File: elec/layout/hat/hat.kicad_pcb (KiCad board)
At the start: 4 copper layers, 108 x 115.9 mm, 85 parts

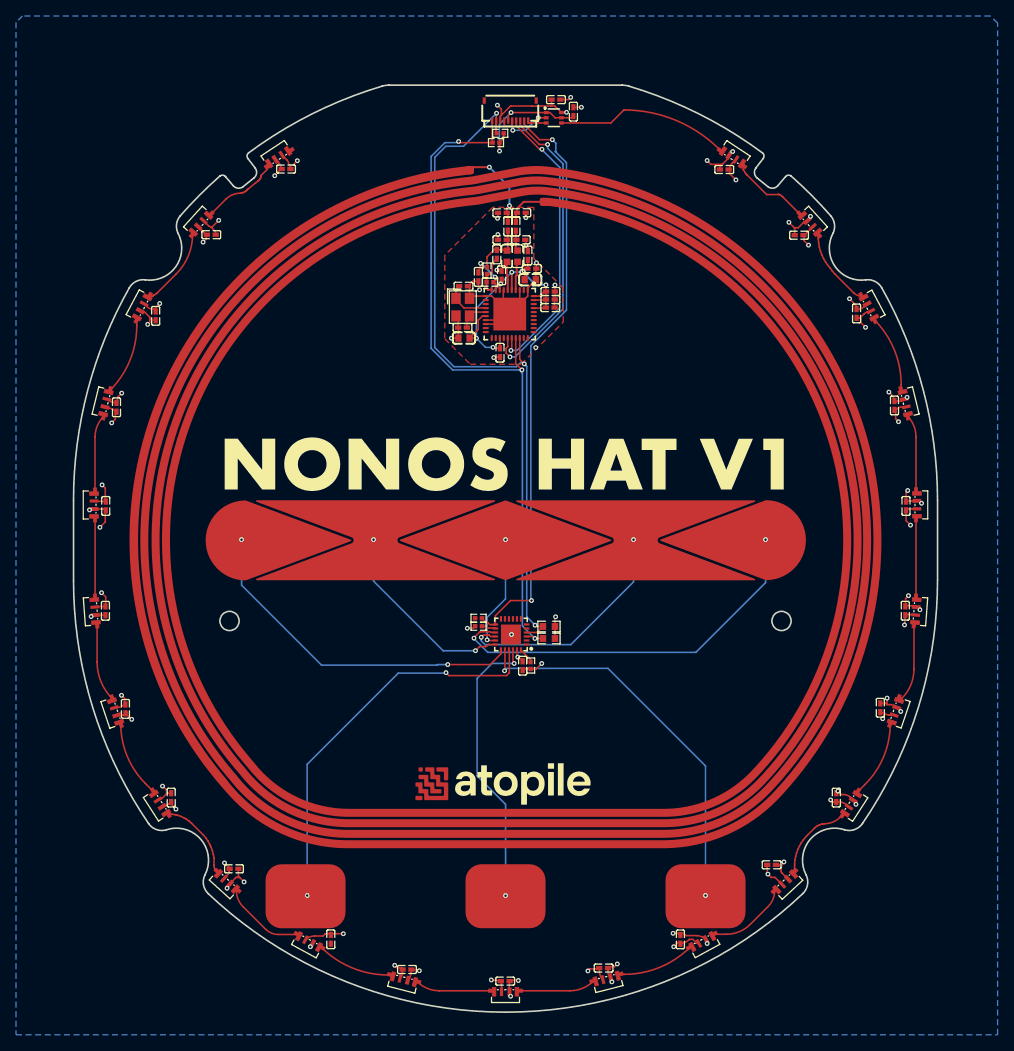
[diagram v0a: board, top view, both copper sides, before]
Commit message: fix via in pad issue
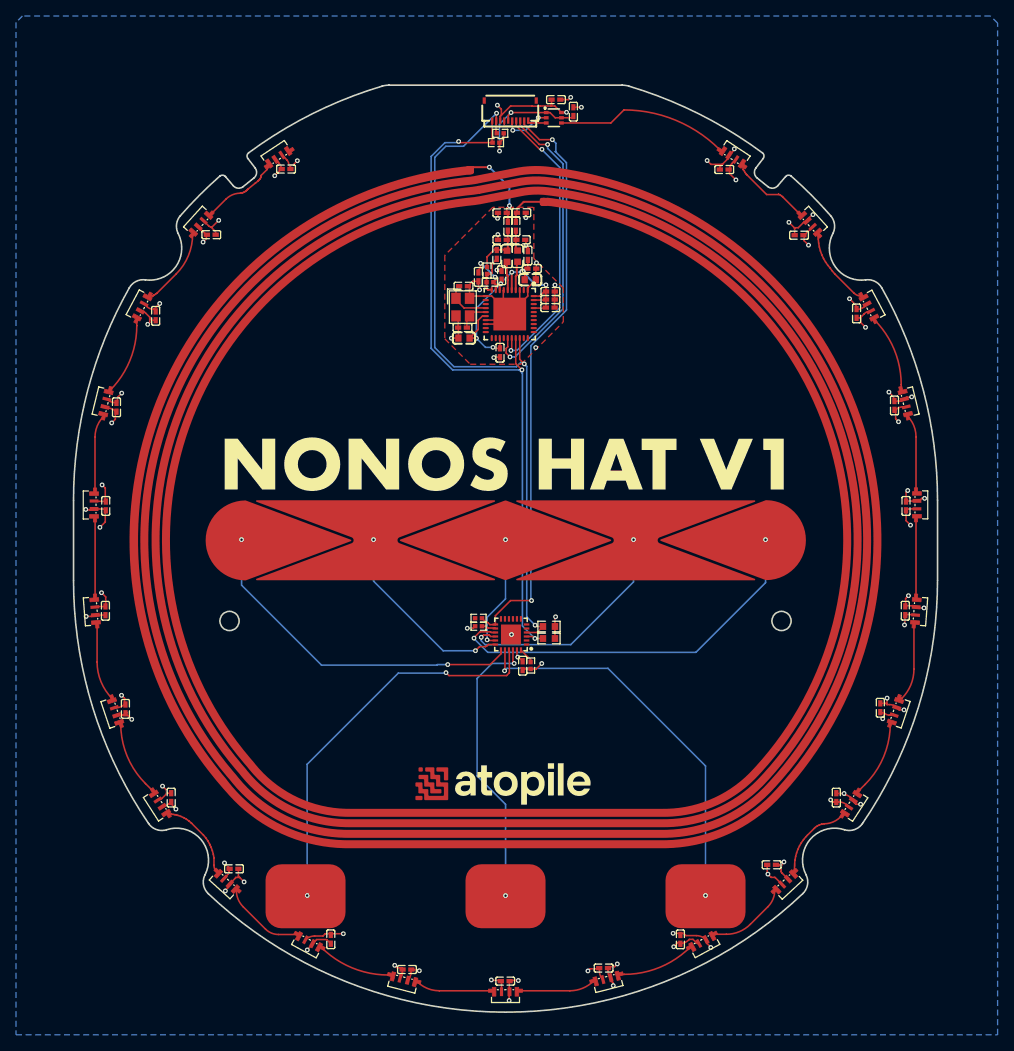
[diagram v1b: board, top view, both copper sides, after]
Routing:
- net hv: track 88.1 -> 97.6 mm

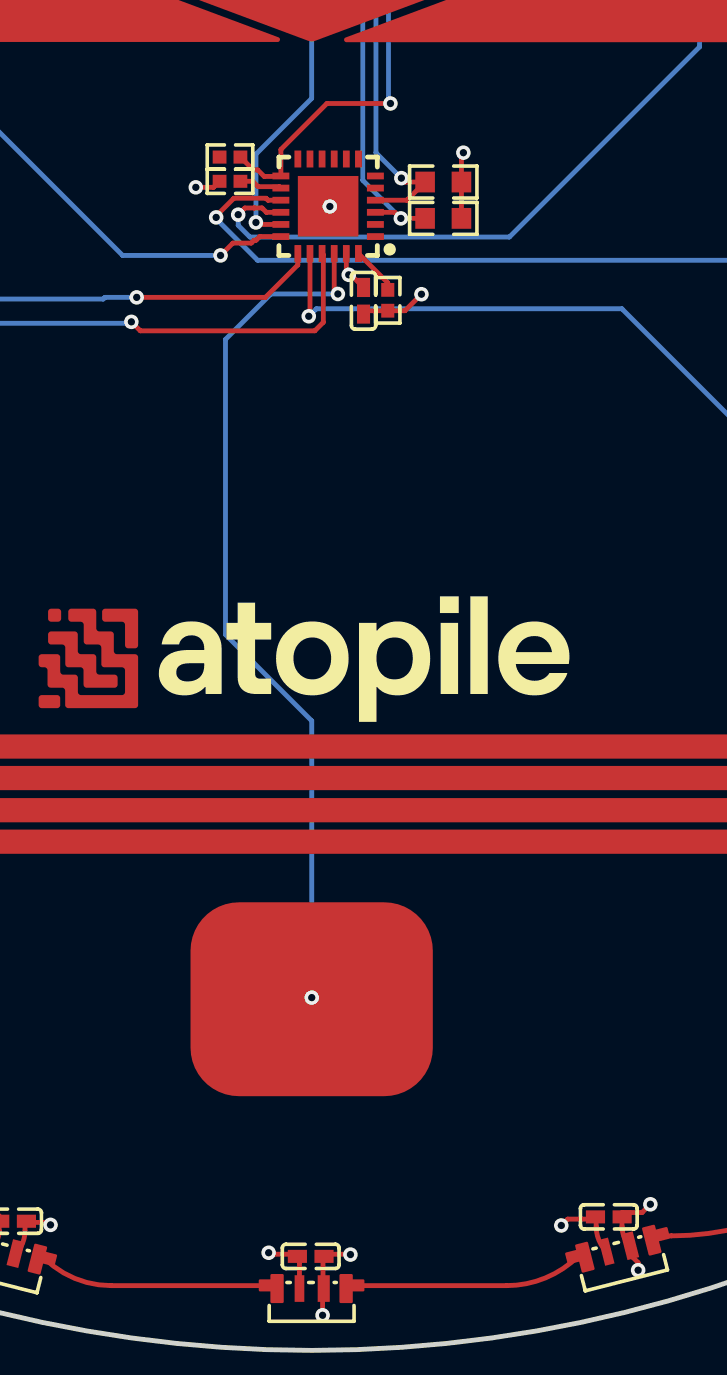
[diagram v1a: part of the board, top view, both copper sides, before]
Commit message: update touch sensor to v0.1.1
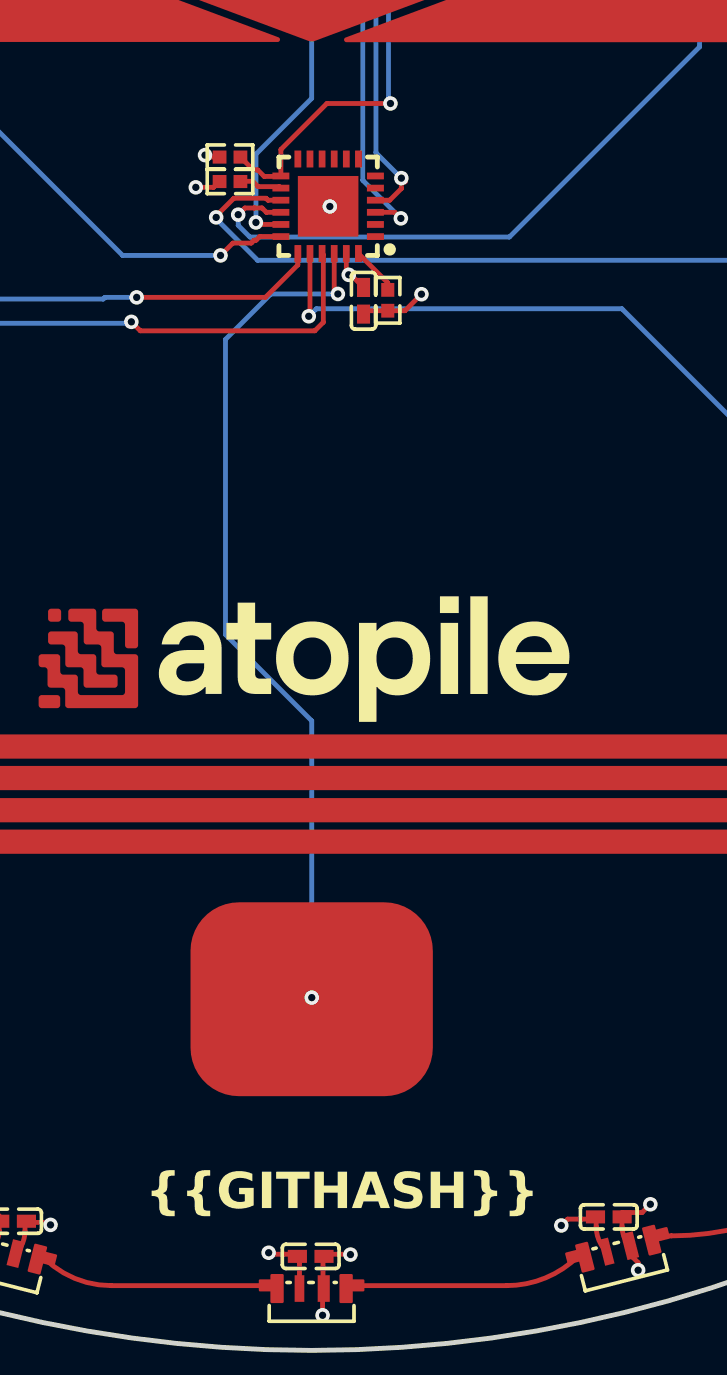
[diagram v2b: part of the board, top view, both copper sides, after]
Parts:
- removed R8, R9: 10kΩ ±1% 100mW, UNI_ROYAL_0603WAF1002T5E:R0603
- R3: value 10kΩ ±1% 62.5mW -> 100kΩ ±1% 62.5mW; footprint UNI_ROYAL_0402WGF1002TCE:R0402 -> UNI_ROYAL_0402WGF1003TCE:R0402
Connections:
- ANT1 pad 10: line -> line-2
- ANT1 pad 9: line-1 -> line-3
- C13 pad 1: line -> line-2
- C14 pad 2: line -> line-2
- C15 pad 1: line-1 -> line-3
- C16 pad 2: line-1 -> line-3
- FPC1 pad 1: NSS_P50_SCL_HSU_RX -> line
- FPC1 pad 2: MOSI_SDA_HSU_TX -> line-1
- R1 pad 1: NSS_P50_SCL_HSU_RX -> line
- R2 pad 1: MOSI_SDA_HSU_TX -> line-1
- R7 pad 2: touch-hv -> hv-1
- U25 pad 3: NSS_P50_SCL_HSU_RX -> line
- U25 pad 4: MOSI_SDA_HSU_TX -> line-1
- U7 pad 27: NSS_P50_SCL_HSU_RX -> line
- U7 pad 28: MOSI_SDA_HSU_TX -> line-1
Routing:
- net MOSI_SDA_HSU_TX: track 90.9 -> 0.00 mm, vias 3 -> 0
- net NSS_P50_SCL_HSU_RX: track 88.7 -> 0.00 mm, vias 3 -> 0
- net line: track 5.42 -> 87.7 mm, vias 0 -> 3
- net line-1: track 10.6 -> 89.4 mm, vias 2 -> 3
- net line-3: track 0.00 -> 10.6 mm, vias 0 -> 2
- net hv-1: track 136.0 -> 144.5 mm
- net line-2: track 0.00 -> 5.42 mm
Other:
- board text added: "{{GITHASH}}"
